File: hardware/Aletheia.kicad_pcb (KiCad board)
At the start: 12 copper layers, 94 x 127 mm, 85 parts, among them J101 Conn_01x04, J201 4090 USB-C, J202 9V battery, SW101 SW_DIP_x08, SW102 SW_DIP_x08, SW104 SW_DIP_x04, SW105 G19AP, SW301 Q/1/STOP, SW302 W/2/CH0, SW303 E/3/CH1, SW304 R/4/CH2, SW305 T/5/CH3, SW306 Y/6/_, SW307 U/7/-, SW308 I/8/+, SW309 O/9/=, SW310 P/0, SW311 A/!/`, SW312 S/"/CH4, SW313 D/$/CH5, SW314 F/%/CH6, SW315 G/^/CH7, SW316 H/&/{, SW317 J/*/}, SW318 K/(/[, SW319 L/)/], SW320 BKSP/DEL, SW321 SHIFT, SW322 Z/\/|, SW323 X/;/:, SW324 C/'/@, SW325 V/#/~, SW326 B/,/<, SW327 N/./>, SW328 M///?, SW329 SYM, SW330 SPC/ENT, U101 W65C02S6TPG-14, U102 AS6C1008-55PCN, U103 W65C22N6TPG-14, U104 74LS04, U105 74LS08, U106 74LS21, U201 LP2954AIT/NOPB, U301 MCP23S17_SP, U302 NHD-0420DZ-NSW-BBW, Y101 ECS-100AX-010

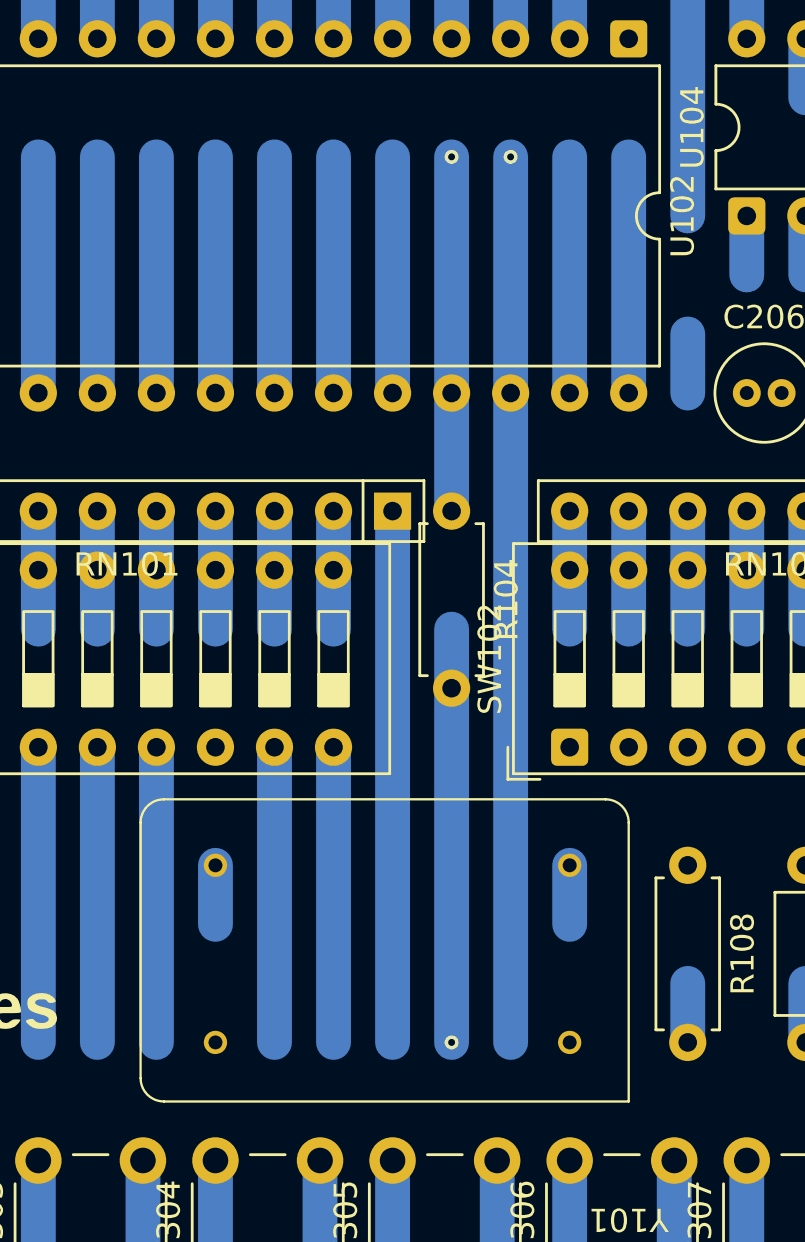
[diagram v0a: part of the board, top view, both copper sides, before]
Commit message: Fix footprint for crystal
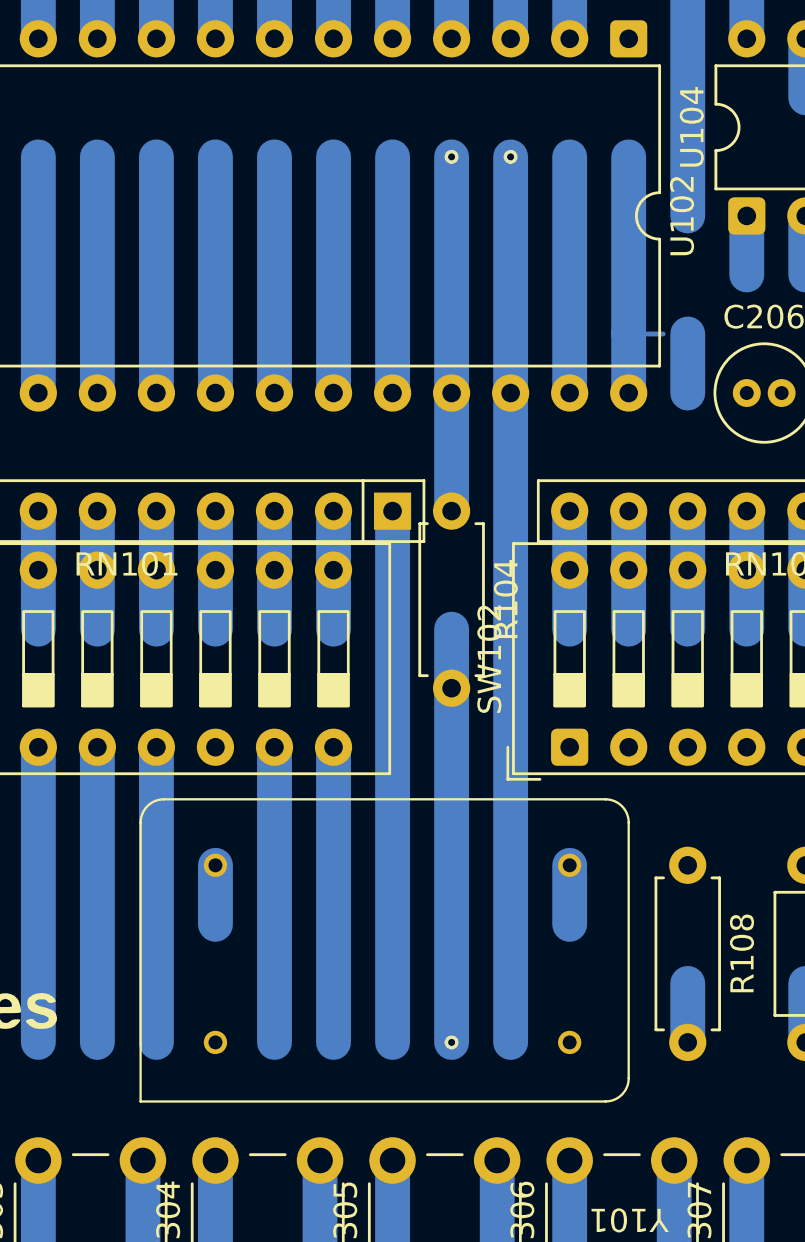
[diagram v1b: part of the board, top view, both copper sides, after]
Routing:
- net VCC: track 535.9 -> 507.9 mm
- net GND: track 792.6 -> 815.0 mm
- net CLOCK: track 126.4 -> 141.6 mm
- net +5V: track 195.3 -> 196.8 mm
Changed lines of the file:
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@@
 		(attr through_hole)
 		(fp_line
-			(start 21 1)
-			(end 21 12)
+			(start 21 12)
+			(end 21 0)
 			(stroke
 				(width 0.1)
@@
 		)
 		(fp_line
-			(start 20 13)
-			(end 1 13)
+			(start 21 0)
+			(end 1 0)
 			(stroke
 				(width 0.1)
@@
 		)
 		(fp_line
-			(start 0 12)
-			(end 0 0)
+			(start 1 13)
+			(end 20 13)
 			(stroke
 				(width 0.1)
@@
 		)
 		(fp_line
-			(start 0 0)
-			(end 20 0)
+			(start 0 1)
+			(end 0 12)
 			(stroke
 				(width 0.1)
@@
 		)
 		(fp_arc
-			(start 20 0)
-			(mid 20.707107 0.292893)
-			(end 21 1)
+			(start 1 13)
+			(mid 0.292893 12.707107)
+			(end 0 12)
 			(stroke
 				(width 0.1)
@@
 		)
 		(fp_arc
-			(start 1 13)
-			(mid 0.292893 12.707107)
-			(end 0 12)
+			(start 0 1)
+			(mid 0.292893 0.292893)
+			(end 1 0)
 			(stroke
 				(width 0.1)
@@
 		)
 		(fp_rect
-			(start 0 0)
-			(end 21 13)
+			(start 21 0)
+			(end 0 13)
 			(stroke
 				(width 0.1)
@@
 		)
 		(pad "1" thru_hole circle
-			(at 2.54 2.54 180)
+			(at 17.78 2.54 180)
 			(size 1 1)
 			(drill 0.6)
@@
 		)
 		(pad "7" thru_hole circle
-			(at 17.78 2.54 180)
+			(at 2.54 2.54 180)
 			(size 1 1)
 			(drill 0.6)
@@
 		)
 		(pad "8" thru_hole circle
-			(at 17.78 10.16 180)
+			(at 2.54 10.16 180)
 			(size 1 1)
 			(drill 0.6)
@@
 		)
 		(pad "14" thru_hole circle
-			(at 2.54 10.16 180)
+			(at 17.78 10.16 180)
 			(size 1 1)
 			(drill 0.6)
@@
 	)
 	(segment
+		(start 93.98 116.84)
+		(end 99.06 116.84)
+		(width 0.2)
+		(layer "In2.Cu")
+		(net 1)
+	)
+	(segment
 		(start 108.18 88.9)
 		(end 111.821 85.259)
@@
 	)
 	(segment
+		(start 93.98 116.84)
+		(end 90.201 120.619)
+		(width 0.2)
+		(layer "In2.Cu")
+		(net 1)
+	)
+	(segment
 		(start 121.92 81.28)
 		(end 121.92 83.82)
@@
 	)
 	(segment
-		(start 83.82 116.84)
-		(end 93.98 116.84)
-		(width 0.2)
-		(layer "In2.Cu")
-		(net 1)
-	)
-	(segment
 		(start 139.7 76.2)
 		(end 142.24 78.74)
@@
 	)
 	(segment
+		(start 90.201 120.619)
+		(end 80.041 120.619)
+		(width 0.2)
+		(layer "In2.Cu")
+		(net 1)
+	)
+	(segment
 		(start 121.33484 105.041)
 		(end 123.559 105.041)
@@
 	)
 	(segment
+		(start 80.041 120.619)
+		(end 74.381 126.279)
+		(width 0.2)
+		(layer "In2.Cu")
+		(net 1)
+	)
+	(segment
 		(start 58.42 78.74)
 		(end 63.5 73.66)
@@
 	)
 	(segment
-		(start 83.82 116.84)
-		(end 74.381 126.279)
-		(width 0.2)
-		(layer "In2.Cu")
-		(net 1)
-	)
-	(segment
 		(start 132.08 73.66)
 		(end 133.181 72.559)
@@
 	)
 	(segment
-		(start 93.98 101.6)
-		(end 117.88 101.6)
+		(start 96.52 119.38)
+		(end 72.10295 119.38)
 		(width 0.2)
 		(layer "In3.Cu")
@@
 	)
 	(segment
-		(start 69.56295 116.84)
-		(end 83.82 116.84)
+		(start 93.98 101.6)
+		(end 117.88 101.6)
 		(width 0.2)
 		(layer "In3.Cu")
@@
 	)
 	(segment
-		(start 60.96 96.52)
-		(end 57.319 100.161)
+		(start 57.319 100.161)
+		(end 60.96 96.52)
 		(width 0.2)
 		(layer "In3.Cu")
@@
 	)
 	(segment
-		(start 57.319 104.59605)
-		(end 69.56295 116.84)
+		(start 99.06 116.84)
+		(end 96.52 119.38)
 		(width 0.2)
 		(layer "In3.Cu")
@@
 	)
 	(segment
+		(start 57.319 104.59605)
+		(end 57.319 100.161)
+		(width 0.2)
+		(layer "In3.Cu")
+		(net 1)
+	)
+	(segment
 		(start 63.5 73.66)
 		(end 63.5 86.36)
@@
 	)
 	(segment
-		(start 57.319 100.161)
+		(start 72.10295 119.38)
 		(end 57.319 104.59605)
 		(width 0.2)
@@
 	)
 	(segment
+		(start 83.82 109.22)
+		(end 83.82 111.76)
+		(width 1.5)
+		(layer "B.Cu")
+		(net 2)
+	)
+	(segment
 		(start 104.14 116.84)
 		(end 104.14 114.3)
@@
 	)
 	(segment
-		(start 99.06 109.22)
-		(end 99.06 111.76)
-		(width 1.5)
-		(layer "B.Cu")
-		(net 2)
-	)
-	(segment
 		(start 122.07 104.844577)
 		(end 122.07 103.435423)
@@
 	)
 	(segment
-		(start 58.42 106.68)
-		(end 96.52 106.68)
-		(width 0.2)
-		(layer "In2.Cu")
-		(net 2)
-	)
-	(segment
-		(start 104.14 114.3)
-		(end 99.06 109.22)
-		(width 0.2)
-		(layer "In2.Cu")
-		(net 2)
-	)
-	(segment
 		(start 128.27 72.39)
 		(end 127 73.66)
@@
 	)
 	(segment
-		(start 96.52 106.68)
-		(end 99.06 109.22)
-		(width 0.2)
-		(layer "In2.Cu")
-		(net 2)
-	)
-	(segment
 		(start 53.34 83.82)
 		(end 55.88 81.28)
@@
 	)
 	(segment
-		(start 104.14 116.84)
-		(end 104.14 114.3)
-		(width 0.2)
-		(layer "In2.Cu")
-		(net 2)
-	)
-	(segment
 		(start 66.04 68.58)
 		(end 67.541 67.079)
@@
 	)
 	(segment
+		(start 83.82 109.22)
+		(end 96.52 109.22)
+		(width 0.2)
+		(layer "In2.Cu")
+		(net 2)
+	)
+	(segment
 		(start 53.34 73.66)
 		(end 55.88 71.12)
@@
 	)
 	(segment
+		(start 96.52 109.22)
+		(end 104.14 116.84)
+		(width 0.2)
+		(layer "In2.Cu")
+		(net 2)
+	)
+	(segment
 		(start 121.92 111.76)
 		(end 116.84 116.84)
@@
 	)
 	(segment
-		(start 83.82 109.22)
-		(end 83.82 111.76)
-		(width 1.5)
-		(layer "B.Cu")
-		(net 18)
-	)
-	(segment
 		(start 60.96 58.42)
 		(end 60.96 63.5)
@@
 	)
 	(segment
+		(start 99.06 109.22)
+		(end 99.06 111.76)
+		(width 1.5)
+		(layer "B.Cu")
+		(net 18)
+	)
+	(segment
 		(start 91.44 35.56)
 		(end 91.44 33.02)
@@
 	)
 	(segment
+		(start 79.72295 106.68)
+		(end 77.639 104.59605)
+		(width 0.2)
+		(layer "In4.Cu")
+		(net 18)
+	)
+	(segment
 		(start 67.141 79.841)
 		(end 67.141 59.521)
@@
 	)
 	(segment
-		(start 83.82 109.22)
-		(end 82.26295 109.22)
-		(width 0.2)
-		(layer "In4.Cu")
-		(net 18)
-	)
-	(segment
-		(start 82.26295 109.22)
-		(end 77.639 104.59605)
+		(start 76.65605 90.001)
+		(end 75.74395 90.001)
 		(width 0.2)
 		(layer "In4.Cu")
@@
 	)
 	(segment
-		(start 76.65605 90.001)
-		(end 75.74395 90.001)
+		(start 99.06 109.22)
+		(end 96.52 106.68)
 		(width 0.2)
 		(layer "In4.Cu")
@@
 	)
 	(segment
+		(start 96.52 106.68)
+		(end 79.72295 106.68)
+		(width 0.2)
+		(layer "In4.Cu")
+		(net 18)
+	)
+	(segment
 		(start 86.36 33.02)
 		(end 86.36 38.1)
@@
 	)
 	(segment
+		(start 101.6 86.36)
+		(end 103.089 86.36)
+		(width 0.2)
+		(layer "B.Cu")
+		(net 36)
+	)
+	(segment
 		(start 129.54 45.72)
 		(end 129.54 63.5)
@@
 	)
 	(segment
-		(start 101.6 88.9)
+		(start 101.6 86.36)
 		(end 101.6 78.74)
 		(width 1.5)
@@
 		(width 1.5)
 		(layer "B.Cu")
+		(net 36)
+	)
+	(segment
+		(start 101.6 88.9)
+		(end 101.6 86.36)
+		(width 1.5)
+		(layer "B.Cu")

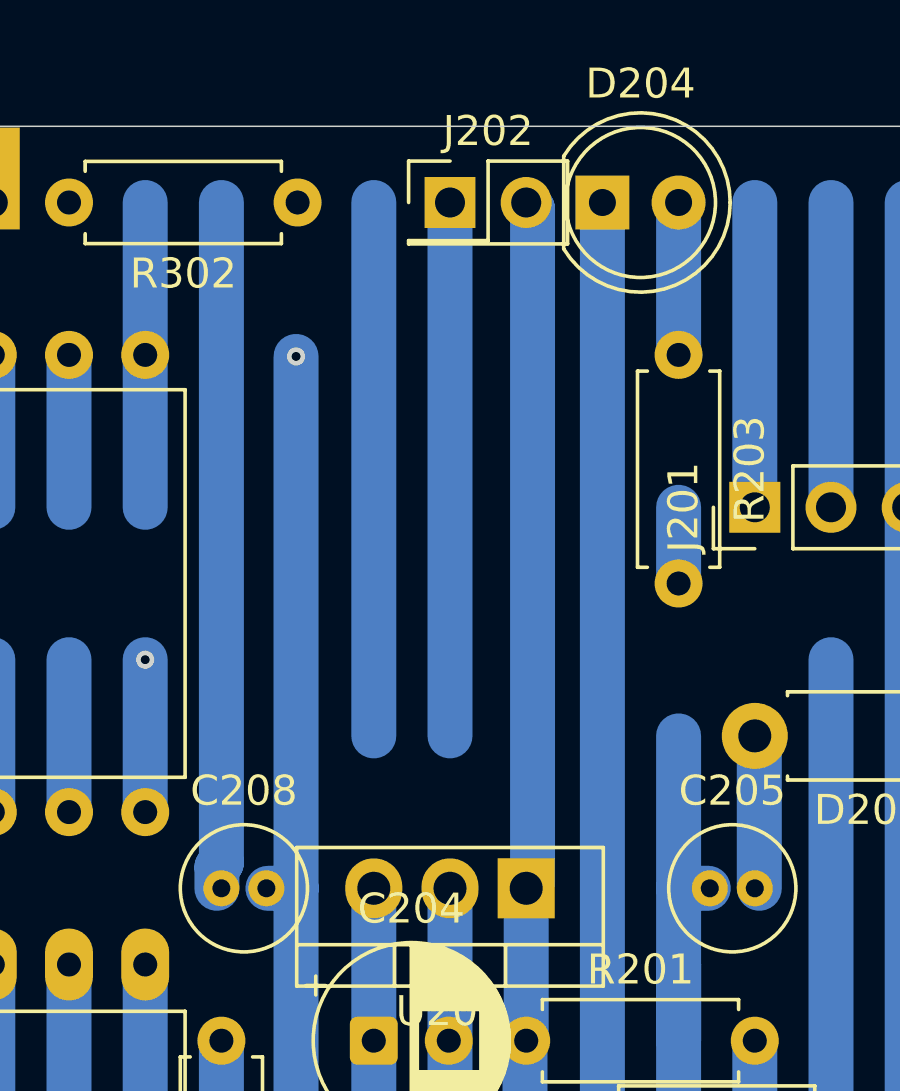
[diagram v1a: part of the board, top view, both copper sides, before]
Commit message: Fix wiring of crystal oscillator
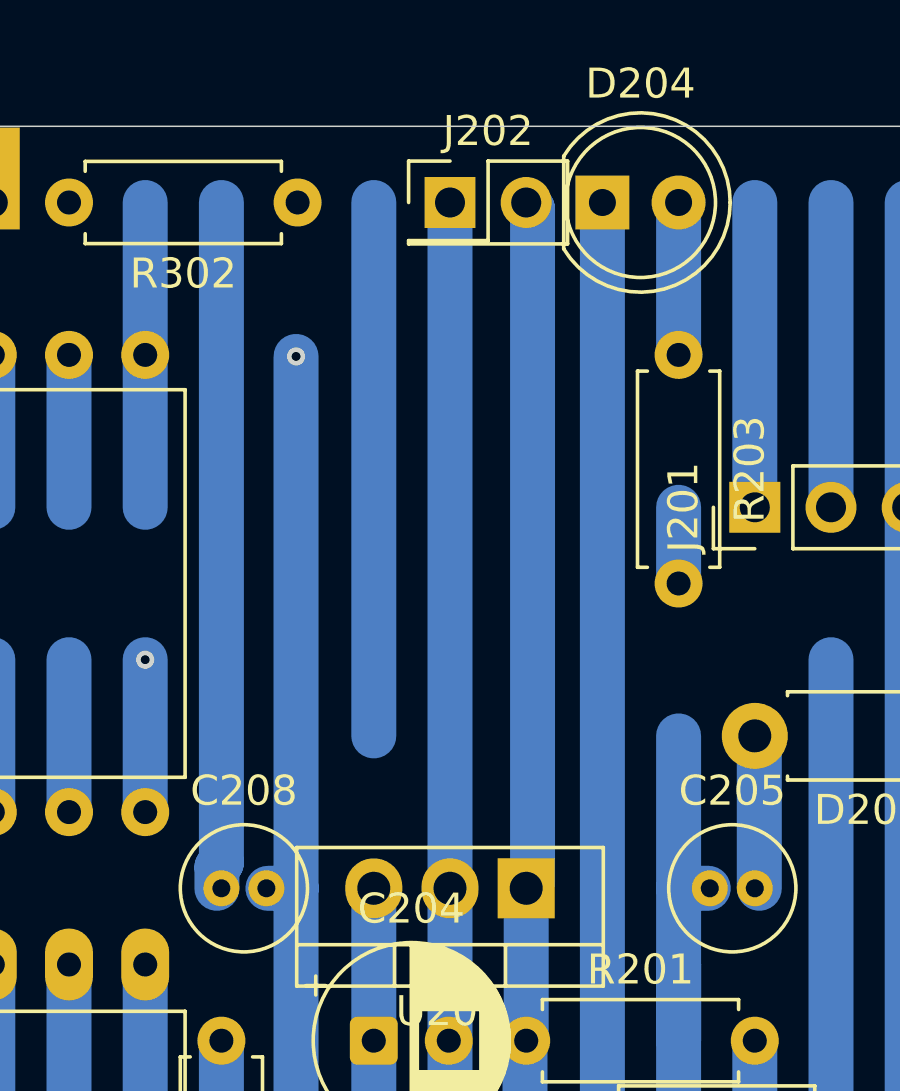
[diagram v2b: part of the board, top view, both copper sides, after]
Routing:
- net GND: track 815.0 -> 820.1 mm
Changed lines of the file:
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@@
-	)
-	(segment
-		(start 111.76 27.94)
-		(end 111.76 45.72)
-		(width 1.5)
-		(layer "B.Cu")
-		(net 1)
 	)
 	(segment
@@
 		(width 1.5)
 		(layer "B.Cu")
+		(net 1)
+	)
+	(segment
+		(start 111.76 27.94)
+		(end 111.76 50.8)
+		(width 1.5)
+		(layer "B.Cu")
